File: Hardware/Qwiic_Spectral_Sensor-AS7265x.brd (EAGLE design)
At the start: 35.6 x 40.6 mm, 50 parts, among them J1 SMD, J2 Serial Interface, J4 SMD, J5 Flash Programming, J8 PTH, U1 AS72651, U3 4MB Flash, U5 AS72653, U6 AS72652

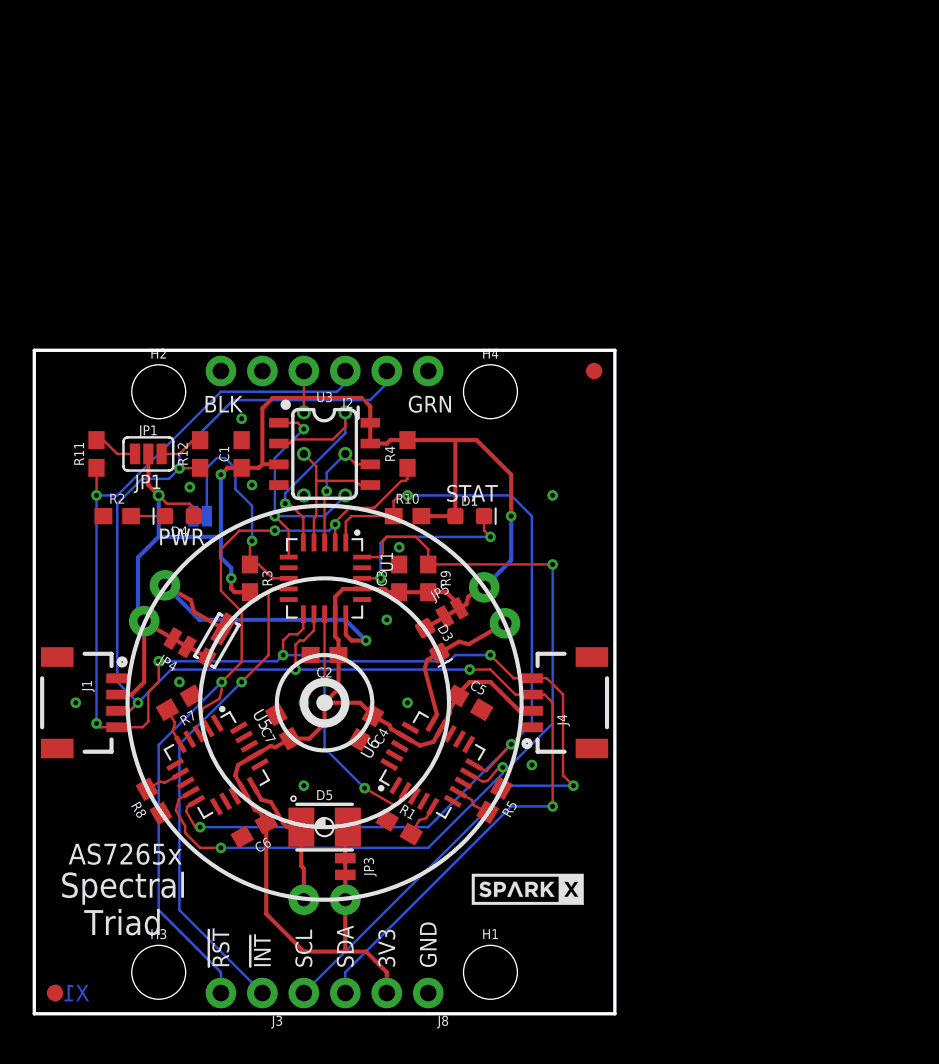
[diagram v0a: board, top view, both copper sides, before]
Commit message: Updating with Buzzard labels. Change logo to SparkFun. Change v to v10.
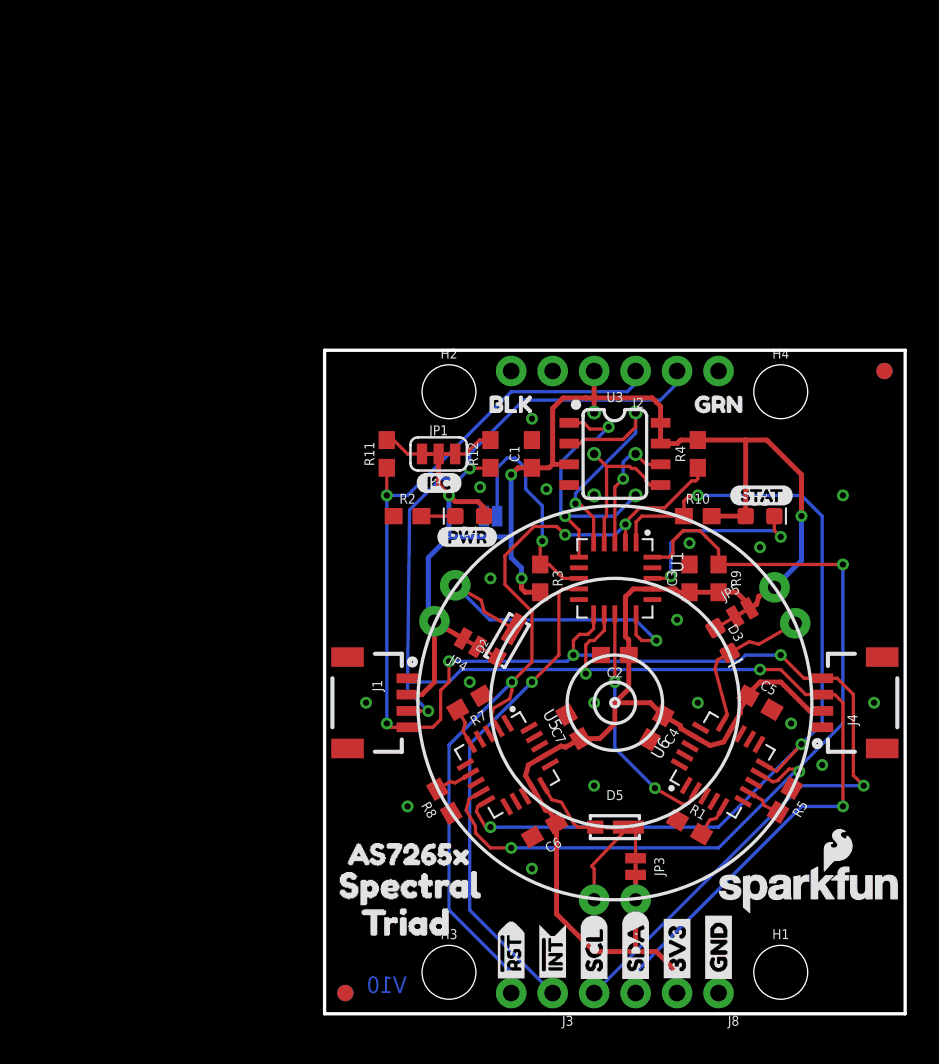
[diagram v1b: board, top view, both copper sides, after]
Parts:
- removed U$1: SPARKX-LOGO3, SparkX:SPARKX-SMALL
- added FD3, FD4: FIDUCIAL1X2, SparkFun-Aesthetics:FIDUCIAL-1X2
- added LOGO1: SFE_LOGO_NAME_FLAME.1_INCH, SparkFun-Aesthetics:SFE_LOGO_NAME_FLAME_.1
- added U$10: (no value), buzzard_labels (50):STAT4
- added U$11, U$12: (no value), buzzard_labels (50):TRIAD2
- added U$13, U$9: (no value), buzzard_labels (50):SPECTRAL1
- added U$14, U$4: (no value), buzzard_labels (50):AS7265X0
- added U$15: (no value), buzzard_labels (51):3V33
- added U$16: (no value), buzzard_labels (51):BLK7
- added U$17: (no value), buzzard_labels (51):GND5
- added U$18: (no value), buzzard_labels (51):GRN6
- added U$19, U$20: (no value), buzzard_labels (51):NC4
- added U$2: (no value), Labels:I_SUPER2_C-()-03
- added U$21: (no value), buzzard_labels (51):RXI2
- added U$22: (no value), buzzard_labels (51):SERIAL0
- added U$23: (no value), buzzard_labels (51):TXO1
- added U$24, U$31: (no value), Labels:3V3-04
- added U$25, U$30: (no value), Labels:GND-04
- added U$26, U$32: (no value), Labels:SDA-[)
- added U$27, U$33: (no value), Labels:SCL-[)
- added U$28, U$34: (no value), Labels:INT#-[<-04
- added U$29, U$35: (no value), Labels:RST#-[>-04
- added U$3: (no value), Labels:PWR-()-03
- added U$5: (no value), buzzard_labels (50):BULB15
- added U$6: (no value), buzzard_labels (50):BULB26
- added U$7: (no value), buzzard_labels (50):BULB37
- added U$8: (no value), buzzard_labels (52):JP20
- BULB1, BULB2, BULB3: value Incandescent -> LEDNS
- D5: device SparkX:PLCC-2 -> SparkX:SUPER_BRIGHT_SMD_LED_1206
- JP1: device SparkFun-Jumpers:SMT-JUMPER_3_2-NC_PASTE_SILK -> SparkFun-Jumpers:SMT-JUMPER_3_2-NC_TRACE_SILK
- moved BULB1 17.8 mm to (7.37, 6.10)
- moved BULB2 17.8 mm to (28.2, 5.97)
- moved BULB3 17.8 mm to (17.8, -12.1)
- moved C1 17.8 mm to (12.7, 15.2)
- moved C2 17.8 mm to (17.8, 2.92)
- moved C3 17.8 mm to (22.4, 7.62)
- moved C5 17.8 mm to (26.7, 0.00)
- moved C6 17.8 mm to (13.5, -7.79)
- moved C7 17.8 mm to (15.3, -1.46)
- moved D1 17.8 mm to (26.7, 11.4)
- moved D2 17.8 mm to (11.2, 3.81)
- moved D3 17.8 mm to (24.4, 3.81)
- moved D4 17.8 mm to (8.89, 11.4)
- moved D5 17.8 mm to (17.8, -7.62)
- moved FD1 17.8 mm to (1.27, -17.8)
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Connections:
- net LED_DRV2: now also D5.C; no longer D5.2
- net N$11: now also D5.A; no longer D5.1
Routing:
- net LED_DRV2: track 8.82 -> 12.0 mm
- net N$11: track 1.97 -> 4.22 mm
- net !CS_EE: track 15.5 -> 17.6 mm
- net TX/SDA: track 91.9 -> 93.1 mm
- net !RST: track 50.0 -> 50.8 mm
- net SCL_S: track 55.6 -> 56.2 mm
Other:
- board text added: "V10"
- board text removed: "!INT"
- board text removed: "!RST"
- board text removed: "3V3"
- board text removed: "AS7265x"
- board text removed: "BLK"
- board text removed: "Bulb1"
- board text removed: "Bulb2"
- board text removed: "Bulb3"
- board text removed: "GRN"
- board text removed: "JP1"
- board text removed: "JP2"
- board text removed: "NC"
- board text removed: "PWR"
- board text removed: "RXI"
- board text removed: "SCL"
- board text removed: "SDA"
- board text removed: "STAT"
- board text removed: "Serial"
- board text removed: "Spectral Triad"
- board text removed: "TXO"
- board text removed: "X10"

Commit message: Removing old files
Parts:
- BULB1, BULB2, BULB3: value LEDNS -> (none)
- D5: device SparkX:SUPER_BRIGHT_SMD_LED_1206 -> SparkFun-LED:PLCC-2
- J1, J4: value SMD -> (none); device SparkX:1X04_1MM_RA -> SparkFun-Connectors:1X04_1MM_RA
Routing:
- net LED_DRV2: track 12.0 -> 8.82 mm
- net N$11: track 4.22 -> 2.06 mm
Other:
- board text removed: "5700K"

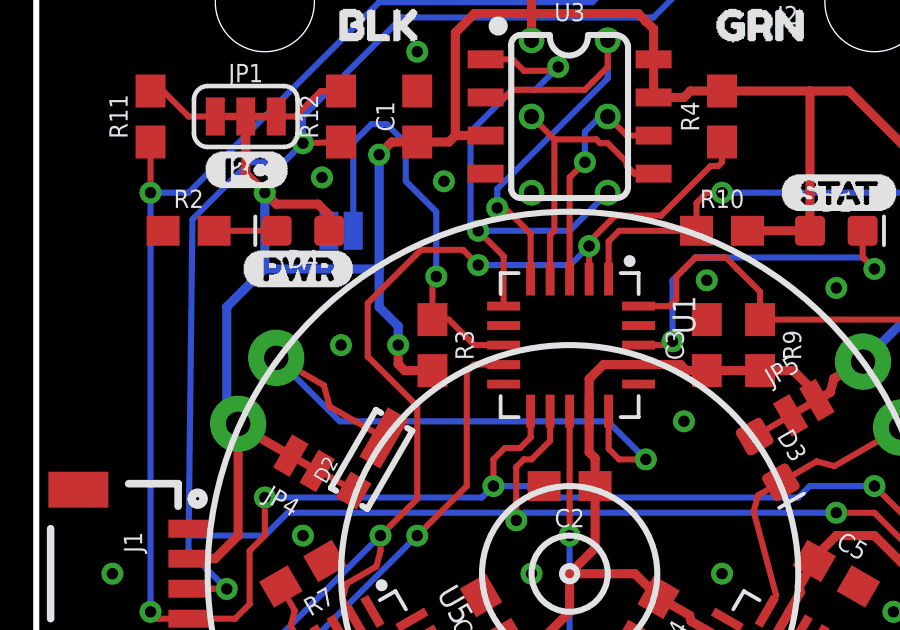
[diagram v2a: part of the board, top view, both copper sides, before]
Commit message: Adding prod_ids to new parts
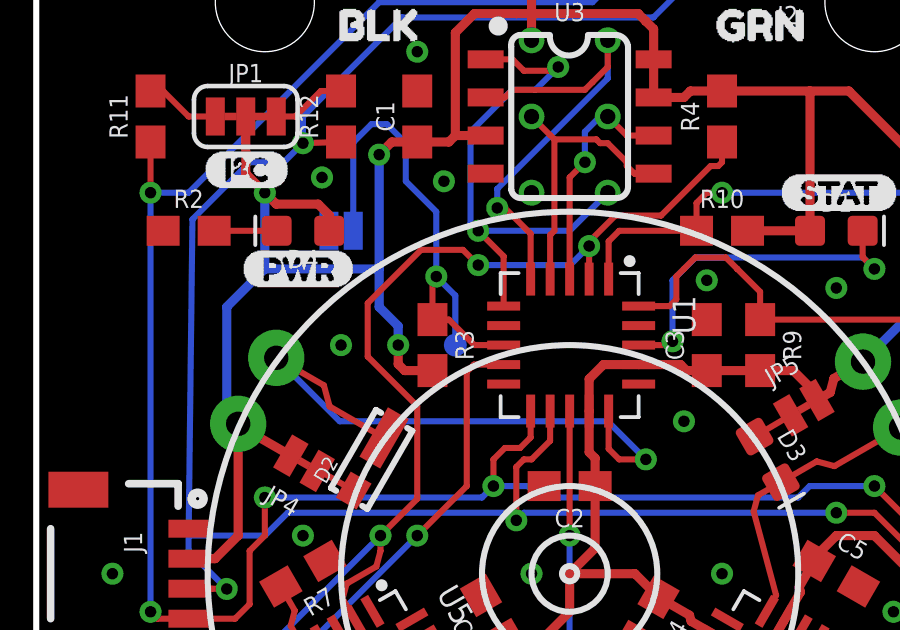
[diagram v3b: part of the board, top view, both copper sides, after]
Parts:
- added TP1: (no value), SparkFun-Connectors:PAD.03X.03
- U1, U5, U6: device AS7265x:LGA20 -> Qwiic_Spectral_Sensor-AS7265x:LGA20
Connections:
- net I2C_ENB: now also TP1.P$1
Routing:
- net I2C_ENB: track 14.3 -> 16.8 mm
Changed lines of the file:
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@@
 <element name="FD1" library="SparkFun-Aesthetics" package="FIDUCIAL-1X2" value="FIDUCIAL1X2" x="1.27" y="-17.78"/>
 <element name="FD2" library="SparkFun-Aesthetics" package="FIDUCIAL-1X2" value="FIDUCIAL1X2" x="34.29" y="20.32"/>
-<element name="U1" library="AS7265x" package="LGA20" value="AS72651" x="17.78" y="7.619953125" smashed="yes" rot="R270">
+<element name="U1" library="Qwiic_Spectral_Sensor-AS7265x" package="LGA20" value="AS72651" x="17.78" y="7.619953125" smashed="yes" rot="R270">
 <attribute name="NAME" x="21.208984375" y="9.270953125" size="0.762" layer="25" rot="R270"/>
 <attribute name="NAME" x="21.209" y="9.270953125" size="0.762" layer="25" rot="R270"/>
 <attribute name="VALUE" x="15.367" y="4.064" size="0.762" layer="27"/>
+<attribute name="PROD_ID" value="IC-14127" x="17.78" y="7.619953125" size="1.778" layer="27" rot="R270" display="off"/>
 </element>
 <element name="R3" library="SparkFun-Resistors" package="0603" value="10k" x="13.2080375" y="7.61996875" rot="R270">
@@
 <attribute name="NAME" x="6.67149375" y="-6.413496875" size="0.6096" layer="25" font="vector" ratio="20" rot="R120" align="bottom-center"/>
 </element>
-<element name="U5" library="AS7265x" package="LGA20" value="AS72653" x="11.18111875" y="-3.80996875" smashed="yes" rot="R300">
+<element name="U5" library="Qwiic_Spectral_Sensor-AS7265x" package="LGA20" value="AS72653" x="11.18111875" y="-3.80996875" smashed="yes" rot="R300">
 <attribute name="NAME" x="13.325221875" y="-0.665659375" size="0.762" layer="25" rot="R300"/>
 <attribute name="NAME" x="13.32521875" y="-0.665659375" size="0.762" layer="25" rot="R300"/>
 <attribute name="VALUE" x="6.858" y="-3.683" size="0.762" layer="27" rot="R300"/>
-</element>
-<element name="U6" library="AS7265x" package="LGA20" value="AS72652" x="24.378890625" y="-3.809965625" smashed="yes" rot="R60">
+<attribute name="PROD_ID" value="IC-14129" x="11.18111875" y="-3.80996875" size="1.778" layer="27" rot="R300" display="off"/>
+</element>
+<element name="U6" library="Qwiic_Spectral_Sensor-AS7265x" package="LGA20" value="AS72652" x="24.378890625" y="-3.809965625" smashed="yes" rot="R60">
 <attribute name="NAME" x="20.5837875" y="-3.525271875" size="0.762" layer="25" rot="R60"/>
 <attribute name="VALUE" x="26.416" y="-7.493" size="0.762" layer="27" rot="R60"/>
 <attribute name="NAME" x="20.5837875" y="-3.525271875" size="0.762" layer="25" rot="R60"/>
+<attribute name="PROD_ID" value="IC-14128" x="24.378890625" y="-3.809965625" size="1.778" layer="27" rot="R60" display="off"/>
 </element>
 <element name="JP5" library="SparkFun-Jumpers" package="SMT-JUMPER_2_NC_TRACE_NO-SILK" value="" x="25.58438125" y="5.5323875" rot="R30">
@@
 <attribute name="PROD_ID" value="DIO-14125" x="24.384" y="3.81" size="1.778" layer="27" font="vector" ratio="15" rot="R300" display="off"/>
 </element>
+<element name="TP1" library="SparkFun-Connectors" package="PAD.03X.03" value="" x="13.97" y="7.62" rot="MR0"/>
 </elements>
 <signals>
@@
 <wire x1="11.176" y1="14.986" x2="10.5664" y2="14.3764" width="0.2032" layer="16"/>
 <wire x1="10.5664" y1="11.43" x2="10.5664" y2="14.3764" width="0.2032" layer="16"/>
+<contactref element="TP1" pad="P$1"/>
+<wire x1="13.97" y1="7.62" x2="13.97" y2="9.2709625" width="0.2032" layer="16"/>
+<wire x1="13.97" y1="9.2709625" x2="13.3350125" y2="9.90595" width="0.2032" layer="16"/>
 </signal>
 <signal name="MISO">

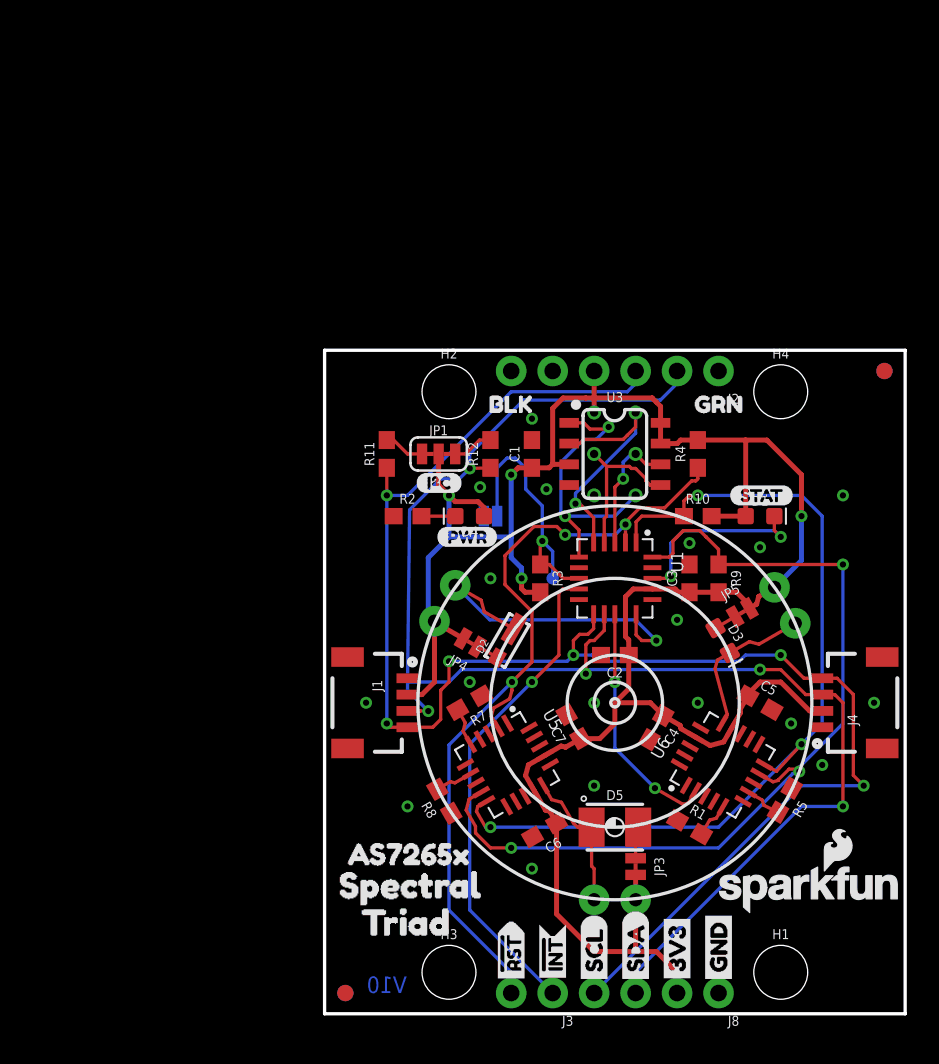
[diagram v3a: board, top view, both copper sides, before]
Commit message: Moving board to origin
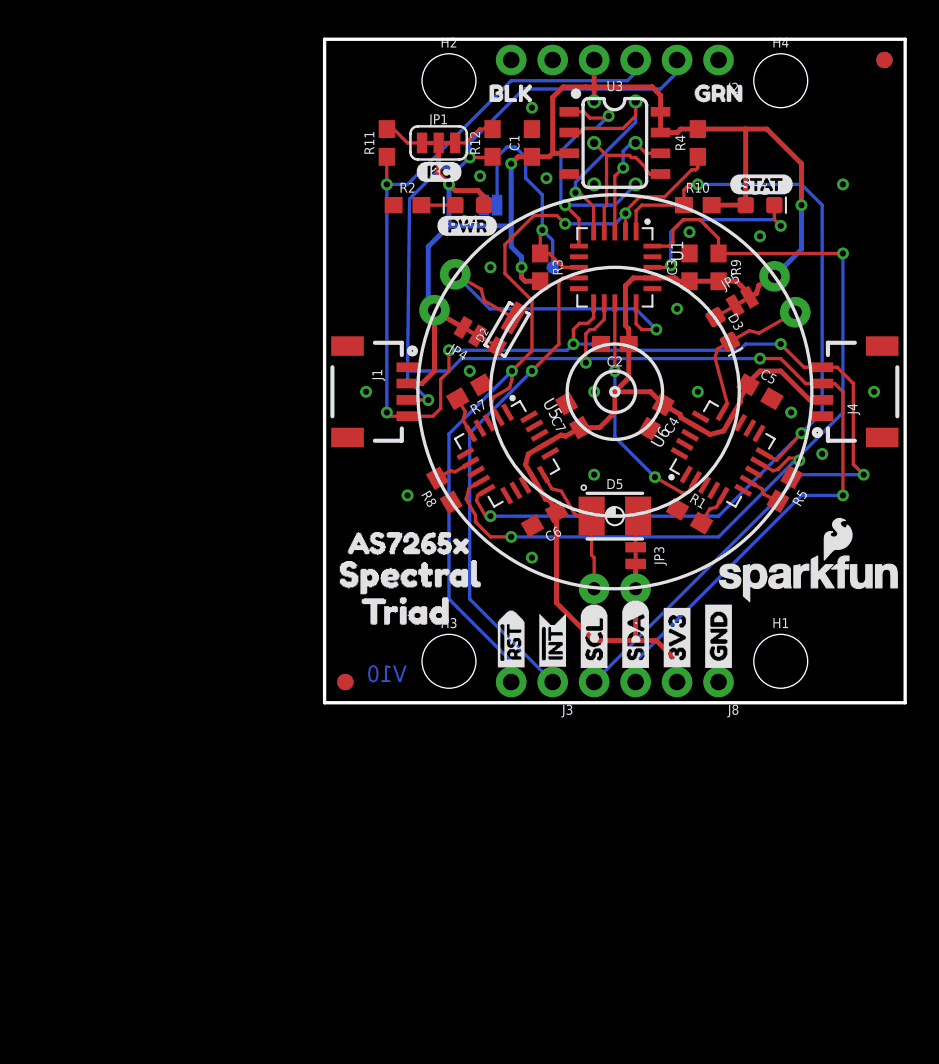
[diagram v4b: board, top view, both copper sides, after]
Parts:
- moved R12 19.1 mm to (10.3, 34.3)
- moved U$19 19.1 mm to (24.1, 34.8)
- moved U$20 19.1 mm to (14.0, 34.8)
- moved U$22 19.1 mm to (21.3, 33.0)
- moved BULB1 19.1 mm to (7.37, 25.1)
- moved BULB2 19.1 mm to (28.2, 25.0)
- moved BULB3 19.1 mm to (17.8, 6.99)
- moved C2 19.1 mm to (17.8, 22.0)
- moved C4 19.1 mm to (20.3, 17.5)
- moved C5 19.1 mm to (26.7, 19.1)
- moved C6 19.1 mm to (13.5, 11.3)
- moved C7 19.1 mm to (15.3, 17.6)
- moved D2 19.1 mm to (11.2, 22.9)
- moved D3 19.1 mm to (24.4, 22.9)
- moved D4 19.1 mm to (8.89, 30.5)
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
